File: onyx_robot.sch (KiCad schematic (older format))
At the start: 30 parts, among them P1 EXT1, P2 EXT2, P3 READER, P4 FTDI, Q1 Q_NMOS_GDS, Q2 Q_NMOS_GDS, SW2 RESET, U1 ADP2301, U2 RELAY_SPDT, U3 ESP-12E

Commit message: Swap 12V in/out connector pins
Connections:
- wire segments 106 -> 107
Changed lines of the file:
@@
 L +12V #PWR013
 U 1 1 55857384
-P 2275 3650
-F 0 "#PWR013" H 2275 3500 50  0001 C CNN
-F 1 "+12V" H 2275 3790 50  0000 C CNN
-F 2 "" H 2275 3650 60  0000 C CNN
-F 3 "" H 2275 3650 60  0000 C CNN
-	1    2275 3650
-	1    0    0    -1
-$EndComp
-Text GLabel 1650 3450 2    60   Input ~ 0
+P 1550 3350
+F 0 "#PWR013" H 1550 3200 50  0001 C CNN
+F 1 "+12V" H 1550 3490 50  0000 C CNN
+F 2 "" H 1550 3350 60  0000 C CNN
+F 3 "" H 1550 3350 60  0000 C CNN
+	1    1550 3350
+	1    0    0    -1
+$EndComp
+Text GLabel 1650 3650 2    60   Input ~ 0
 12V_OUT
 Text GLabel 1650 5100 2    60   Input ~ 0
@@
 Connection ~ 1550 5000
 Wire Wire Line
-	1450 3450 1650 3450
-Wire Wire Line
-	1450 3650 2275 3650
+	1450 3650 1650 3650
 Wire Wire Line
 	1450 3550 1550 3550
@@
 	4025 1800 4025 1525
 Connection ~ 4025 1525
+Wire Wire Line
+	1450 3450 1550 3450
+Wire Wire Line
+	1550 3450 1550 3350
 $EndSCHEMATC

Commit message: Switch to standard (not hand-soldering) footprints to save space
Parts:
- C1, C2: footprint Capacitors_SMD:C_1206_HandSoldering -> Capacitors_SMD:C_1206
- C3, C4: footprint Capacitors_SMD:C_0603_HandSoldering -> Capacitors_SMD:C_0603
- D1, D2: footprint Diodes_SMD:Diode-SMA_Handsoldering -> Diodes_SMD:Diode-SMA_Standard
- Q1, Q2: footprint Housings_SOT-23_SOT-143_TSOT-6:SOT-23_Handsoldering -> Housings_SOT-23_SOT-143_TSOT-6:SOT-23
- R1, R10, R11, R2, R3, R4, R5, R6, R7, R8, R9: footprint Resistors_SMD:R_0603_HandSoldering -> Resistors_SMD:R_0603
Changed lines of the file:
@@
 F 0 "R6" V 6905 4425 50  0000 C CNN
 F 1 "10K" V 6825 4425 50  0000 C CNN
-F 2 "Resistors_SMD:R_0603_HandSoldering" V 6755 4425 30  0001 C CNN
+F 2 "Resistors_SMD:R_0603" V 6755 4425 30  0001 C CNN
 F 3 "" H 6825 4425 30  0000 C CNN
 	1    6825 4425
@@
 F 0 "R10" V 9905 4675 50  0000 C CNN
 F 1 "10K" V 9825 4675 50  0000 C CNN
-F 2 "Resistors_SMD:R_0603_HandSoldering" V 9755 4675 30  0001 C CNN
+F 2 "Resistors_SMD:R_0603" V 9755 4675 30  0001 C CNN
 F 3 "" H 9825 4675 30  0000 C CNN
 	1    9825 4675
@@
 F 0 "R7" V 7130 1700 50  0000 C CNN
 F 1 "10K 1%" V 6975 1700 50  0000 C CNN
-F 2 "Resistors_SMD:R_0603_HandSoldering" V 6980 1700 30  0001 C CNN
+F 2 "Resistors_SMD:R_0603" V 6980 1700 30  0001 C CNN
 F 3 "" H 7050 1700 30  0000 C CNN
 	1    7050 1700
@@
 F 0 "R8" V 7130 2125 50  0000 C CNN
 F 1 "2K2 1%" V 6975 2125 50  0000 C CNN
-F 2 "Resistors_SMD:R_0603_HandSoldering" V 6980 2125 30  0001 C CNN
+F 2 "Resistors_SMD:R_0603" V 6980 2125 30  0001 C CNN
 F 3 "" H 7050 2125 30  0000 C CNN
 	1    7050 2125
@@
 F 0 "R11" V 10180 1600 50  0000 C CNN
 F 1 "10K" V 10100 1600 50  0000 C CNN
-F 2 "Resistors_SMD:R_0603_HandSoldering" V 10030 1600 30  0001 C CNN
+F 2 "Resistors_SMD:R_0603" V 10030 1600 30  0001 C CNN
 F 3 "" H 10100 1600 30  0000 C CNN
 	1    10100 1600
@@
 F 0 "R9" V 8780 1550 50  0000 C CNN
 F 1 "10K" V 8700 1550 50  0000 C CNN
-F 2 "Resistors_SMD:R_0603_HandSoldering" V 8630 1550 30  0001 C CNN
+F 2 "Resistors_SMD:R_0603" V 8630 1550 30  0001 C CNN
 F 3 "" H 8700 1550 30  0000 C CNN
 	1    8700 1550
@@
 F 0 "Q1" H 4125 4650 50  0000 R CNN
 F 1 "Q_NMOS_GDS" H 4475 4550 50  0000 R CNN
-F 2 "Housings_SOT-23_SOT-143_TSOT-6:SOT-23_Handsoldering" H 4025 4700 29  0001 C CNN
+F 2 "Housings_SOT-23_SOT-143_TSOT-6:SOT-23" H 4025 4700 29  0001 C CNN
 F 3 "" H 3825 4600 60  0000 C CNN
 	1    3825 4600
@@
 F 0 "D2" H 3925 4100 50  0000 C CNN
 F 1 "D" H 3925 3900 50  0000 C CNN
-F 2 "Diodes_SMD:Diode-SMA_Handsoldering" H 3925 4000 60  0001 C CNN
+F 2 "Diodes_SMD:Diode-SMA_Standard" H 3925 4000 60  0001 C CNN
 F 3 "" H 3925 4000 60  0000 C CNN
 	1    3925 4000
@@
 F 0 "R5" V 3655 4800 50  0000 C CNN
 F 1 "10K" V 3575 4800 50  0000 C CNN
-F 2 "Resistors_SMD:R_0603_HandSoldering" V 3505 4800 30  0001 C CNN
+F 2 "Resistors_SMD:R_0603" V 3505 4800 30  0001 C CNN
 F 3 "" H 3575 4800 30  0000 C CNN
 	1    3575 4800
@@
 F 0 "C1" H 1300 1800 50  0000 L CNN
 F 1 "10uF 25V" H 1075 1600 50  0000 L CNN
-F 2 "Capacitors_SMD:C_1206_HandSoldering" H 1313 1550 30  0001 C CNN
+F 2 "Capacitors_SMD:C_1206" H 1313 1550 30  0001 C CNN
 F 3 "" H 1275 1700 60  0000 C CNN
 	1    1275 1700
@@
 F 0 "R3" V 1655 1500 50  0000 C CNN
 F 1 "56K 1%" V 1500 1500 50  0000 C CNN
-F 2 "Resistors_SMD:R_0603_HandSoldering" V 1505 1500 30  0001 C CNN
+F 2 "Resistors_SMD:R_0603" V 1505 1500 30  0001 C CNN
 F 3 "" H 1575 1500 30  0000 C CNN
 	1    1575 1500
@@
 F 0 "R4" V 1655 2075 50  0000 C CNN
 F 1 "10K2 1%" V 1500 2075 50  0000 C CNN
-F 2 "Resistors_SMD:R_0603_HandSoldering" V 1505 2075 30  0001 C CNN
+F 2 "Resistors_SMD:R_0603" V 1505 2075 30  0001 C CNN
 F 3 "" H 1575 2075 30  0000 C CNN
 	1    1575 2075
@@
 F 0 "C3" H 2900 1475 50  0000 L CNN
 F 1 "0.1uF 6.3V" H 3000 1375 50  0000 L CNN
-F 2 "Capacitors_SMD:C_0603_HandSoldering" H 2913 1225 30  0001 C CNN
+F 2 "Capacitors_SMD:C_0603" H 2913 1225 30  0001 C CNN
 F 3 "" H 2875 1375 60  0000 C CNN
 	1    2875 1375
@@
 F 0 "C2" H 4050 2050 50  0000 L CNN
 F 1 "22uF 6.3V" H 4050 1850 50  0000 L CNN
-F 2 "Capacitors_SMD:C_1206_HandSoldering" H 4063 1800 30  0001 C CNN
+F 2 "Capacitors_SMD:C_1206" H 4063 1800 30  0001 C CNN
 F 3 "" H 4025 1950 60  0000 C CNN
 	1    4025 1950
@@
 F 0 "R1" V 3805 1675 50  0000 C CNN
 F 1 "31K6 1%" H 3500 1600 50  0000 C CNN
-F 2 "Resistors_SMD:R_0603_HandSoldering" V 3655 1675 30  0001 C CNN
+F 2 "Resistors_SMD:R_0603" V 3655 1675 30  0001 C CNN
 F 3 "" H 3725 1675 30  0000 C CNN
 	1    3725 1675
@@
 F 0 "R2" V 3805 2075 50  0000 C CNN
 F 1 "20K2 1%" V 3650 2075 50  0000 C CNN
-F 2 "Resistors_SMD:R_0603_HandSoldering" V 3655 2075 30  0001 C CNN
+F 2 "Resistors_SMD:R_0603" V 3655 2075 30  0001 C CNN
 F 3 "" H 3725 2075 30  0000 C CNN
 	1    3725 2075
@@
 F 0 "D1" H 2875 2175 50  0000 C CNN
 F 1 "B230A" H 2875 1975 50  0000 C CNN
-F 2 "Diodes_SMD:Diode-SMA_Handsoldering" H 2875 2075 60  0001 C CNN
+F 2 "Diodes_SMD:Diode-SMA_Standard" H 2875 2075 60  0001 C CNN
 F 3 "" H 2875 2075 60  0000 C CNN
 	1    2875 2075
@@
 F 0 "C4" H 6850 5025 50  0000 L CNN
 F 1 "0.1uF" H 6850 4825 50  0000 L CNN
-F 2 "Capacitors_SMD:C_0603_HandSoldering" H 6863 4775 30  0001 C CNN
+F 2 "Capacitors_SMD:C_0603" H 6863 4775 30  0001 C CNN
 F 3 "" H 6825 4925 60  0000 C CNN
 	1    6825 4925
@@
 F 0 "Q2" H 9250 1900 50  0000 R CNN
 F 1 "Q_NMOS_GDS" H 9600 1800 50  0000 R CNN
-F 2 "Housings_SOT-23_SOT-143_TSOT-6:SOT-23_Handsoldering" H 9150 1950 29  0001 C CNN
+F 2 "Housings_SOT-23_SOT-143_TSOT-6:SOT-23" H 9150 1950 29  0001 C CNN
 F 3 "" H 8950 1850 60  0000 C CNN
 	1    8950 1850

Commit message: Use corrected ESP-12E footprint
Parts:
- U3: footprint jdunmire-kicad-ESP8266:ESP-12E -> timhawes:ESP-12E
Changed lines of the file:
@@
 F 0 "U3" H 8600 4175 50  0000 C CNN
 F 1 "ESP-12E" H 8600 4375 50  0000 C CNN
-F 2 "jdunmire-kicad-ESP8266:ESP-12E" H 8600 4275 50  0001 C CNN
+F 2 "timhawes:ESP-12E" H 8600 4275 50  0001 C CNN
 F 3 "" H 8600 4275 50  0001 C CNN
 	1    8600 4275

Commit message: Shuffle READER pins to put GND/3.3V together
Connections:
- wire segments 107 -> 129
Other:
- moved on the sheet: P3, P4
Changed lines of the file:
@@
 L CONN_01X06 P4
 U 1 1 55847D6C
-P 2950 6525
-F 0 "P4" H 2950 6875 50  0000 C CNN
-F 1 "FTDI" V 3050 6525 50  0000 C CNN
-F 2 "Pin_Headers:Pin_Header_Straight_1x06" H 2950 6525 60  0001 C CNN
-F 3 "" H 2950 6525 60  0000 C CNN
-	1    2950 6525
+P 3100 6525
+F 0 "P4" H 3100 6875 50  0000 C CNN
+F 1 "FTDI" V 3200 6525 50  0000 C CNN
+F 2 "Pin_Headers:Pin_Header_Straight_1x06" H 3100 6525 60  0001 C CNN
+F 3 "" H 3100 6525 60  0000 C CNN
+	1    3100 6525
 	-1   0    0    1
 $EndComp
@@
 L CONN_01X08 P3
 U 1 1 55847F14
-P 1250 6425
-F 0 "P3" H 1250 6875 50  0000 C CNN
-F 1 "READER" V 1350 6425 50  0000 C CNN
-F 2 "timhawes:Terminal_Block_5.08mm_x8" H 1250 6425 60  0001 C CNN
-F 3 "" H 1250 6425 60  0000 C CNN
-	1    1250 6425
+P 1250 6525
+F 0 "P3" H 1250 6975 50  0000 C CNN
+F 1 "READER" V 1350 6525 50  0000 C CNN
+F 2 "timhawes:Terminal_Block_5.08mm_x8" H 1250 6525 60  0001 C CNN
+F 3 "" H 1250 6525 60  0000 C CNN
+	1    1250 6525
 	-1   0    0    1
 $EndComp
@@
 Text GLabel 9600 4075 2    60   Input ~ 0
 RX
-Text GLabel 3200 6475 2    60   Input ~ 0
+Text GLabel 3350 6475 2    60   Input ~ 0
 TX
-Text GLabel 3375 6375 2    60   Input ~ 0
+Text GLabel 3525 6375 2    60   Input ~ 0
 RX
 $Comp
 L +3.3V #PWR09
 U 1 1 5584AC0A
-P 3725 6575
-F 0 "#PWR09" H 3725 6425 50  0001 C CNN
-F 1 "+3.3V" H 3725 6715 50  0000 C CNN
-F 2 "" H 3725 6575 60  0000 C CNN
-F 3 "" H 3725 6575 60  0000 C CNN
-	1    3725 6575
+P 3875 6575
+F 0 "#PWR09" H 3875 6425 50  0001 C CNN
+F 1 "+3.3V" H 3875 6715 50  0000 C CNN
+F 2 "" H 3875 6575 60  0000 C CNN
+F 3 "" H 3875 6575 60  0000 C CNN
+	1    3875 6575
 	-1   0    0    -1
 $EndComp
-NoConn ~ 3150 6675
-NoConn ~ 3150 6275
-Text GLabel 1550 6475 2    60   Input ~ 0
+NoConn ~ 3300 6675
+NoConn ~ 3300 6275
+Text GLabel 1500 6475 2    60   Input ~ 0
 MOSI
-Text GLabel 1875 6575 2    60   Input ~ 0
+Text GLabel 1825 6575 2    60   Input ~ 0
 MISO
-Text GLabel 1875 6375 2    60   Input ~ 0
+Text GLabel 1825 6375 2    60   Input ~ 0
 CS
-Text GLabel 1550 6675 2    60   Input ~ 0
+Text GLabel 1500 6675 2    60   Input ~ 0
 CLK
-Text GLabel 1875 6175 2    60   Input ~ 0
+Text GLabel 1825 6175 2    60   Input ~ 0
 PIEZO
 $Comp
 L +3.3V #PWR010
 U 1 1 5584BDD3
-P 1550 5975
-F 0 "#PWR010" H 1550 5825 50  0001 C CNN
-F 1 "+3.3V" H 1550 6115 50  0000 C CNN
-F 2 "" H 1550 5975 60  0000 C CNN
-F 3 "" H 1550 5975 60  0000 C CNN
-	1    1550 5975
-	1    0    0    -1
-$EndComp
-Text GLabel 1550 6275 2    60   Input ~ 0
+P 2325 6675
+F 0 "#PWR010" H 2325 6525 50  0001 C CNN
+F 1 "+3.3V" H 2325 6815 50  0000 C CNN
+F 2 "" H 2325 6675 60  0000 C CNN
+F 3 "" H 2325 6675 60  0000 C CNN
+	1    2325 6675
+	1    0    0    -1
+$EndComp
+Text GLabel 1500 6275 2    60   Input ~ 0
 LED
 $Comp
@@
 L GND #PWR029
 U 1 1 558E4075
-P 3250 6875
-F 0 "#PWR029" H 3250 6625 50  0001 C CNN
-F 1 "GND" H 3250 6725 50  0000 C CNN
-F 2 "" H 3250 6875 60  0000 C CNN
-F 3 "" H 3250 6875 60  0000 C CNN
-	1    3250 6875
+P 3400 6875
+F 0 "#PWR029" H 3400 6625 50  0001 C CNN
+F 1 "GND" H 3400 6725 50  0000 C CNN
+F 2 "" H 3400 6875 60  0000 C CNN
+F 3 "" H 3400 6875 60  0000 C CNN
+	1    3400 6875
 	1    0    0    -1
 $EndComp
@@
 	7050 1550 7050 1500
 Wire Wire Line
-	7050 1850 7050 1975
+	7050 1850 7050 1900
+Wire Wire Line
+	7050 1900 7050 1975
 Wire Wire Line
 	7050 2275 7050 2350
@@
 	10100 1350 10100 1450
 Wire Wire Line
-	10100 1750 10100 1850
+	10100 1750 10100 1800
+Wire Wire Line
+	10100 1800 10100 1850
 Wire Wire Line
 	10400 1800 10100 1800
@@
 	10100 2450 10100 2550
 Wire Wire Line
-	6750 4675 7700 4675
+	6750 4675 6825 4675
+Wire Wire Line
+	6825 4675 7700 4675
 Wire Wire Line
 	7350 3975 7700 3975
@@
 	6825 4175 6825 4275
 Wire Wire Line
-	6825 4575 6825 4775
+	6825 4575 6825 4675
+Wire Wire Line
+	6825 4675 6825 4775
 Connection ~ 6825 4675
 Wire Wire Line
-	9500 4675 9675 4675
+	9500 4675 9575 4675
+Wire Wire Line
+	9575 4675 9675 4675
 Wire Wire Line
 	9575 4675 9575 4750
@@
 	7700 4075 7625 4075
 Wire Wire Line
-	9500 4575 10300 4575
+	9500 4575 10125 4575
+Wire Wire Line
+	10125 4575 10300 4575
 Wire Wire Line
 	9825 3975 9500 3975
@@
 	9600 4475 9500 4475
 Wire Wire Line
-	3375 6375 3150 6375
-Wire Wire Line
-	3725 6575 3150 6575
-Wire Wire Line
-	3475 4600 3625 4600
+	3525 6375 3300 6375
+Wire Wire Line
+	3875 6575 3300 6575
+Wire Wire Line
+	3475 4600 3575 4600
+Wire Wire Line
+	3575 4600 3625 4600
 Wire Wire Line
 	3575 4600 3575 4650
 Connection ~ 3575 4600
 Wire Wire Line
-	3925 4800 3925 5050
+	3925 4800 3925 5000
+Wire Wire Line
+	3925 5000 3925 5050
 Wire Wire Line
 	3575 4950 3575 5000
@@
 	3925 4150 3925 4400
 Wire Wire Line
-	3925 3525 3925 3850
+	3925 3525 3925 3600
+Wire Wire Line
+	3925 3600 3925 3850
 Wire Wire Line
 	3925 3850 4100 3850
@@
 	5425 4150 5375 4150
 Wire Wire Line
-	1275 1100 1275 1550
+	1275 1100 1275 1225
+Wire Wire Line
+	1275 1225 1275 1550
 Connection ~ 1275 1225
 Wire Wire Line
@@
 Connection ~ 1575 1225
 Wire Wire Line
-	1575 1650 1575 1925
+	1575 1650 1575 1825
+Wire Wire Line
+	1575 1825 1575 1925
 Wire Wire Line
 	1575 1825 1725 1825
 Connection ~ 1575 1825
 Wire Wire Line
-	1575 2225 1575 2325
+	1575 2225 1575 2275
+Wire Wire Line
+	1575 2275 1575 2325
 Wire Wire Line
 	1275 1850 1275 2275
@@
 	2725 1225 2875 1225
 Wire Wire Line
-	2725 1525 3050 1525
+	2725 1525 2875 1525
+Wire Wire Line
+	2875 1525 3050 1525
 Wire Wire Line
 	2875 1525 2875 1925
@@
 Connection ~ 2875 1525
 Wire Wire Line
-	3650 1525 4300 1525
+	3650 1525 3725 1525
+Wire Wire Line
+	3725 1525 4025 1525
+Wire Wire Line
+	4025 1525 4300 1525
 Connection ~ 3725 1525
 Connection ~ 3725 1825
@@
 	4025 2100 4025 2325
 Wire Wire Line
-	1275 1225 1725 1225
+	1275 1225 1575 1225
+Wire Wire Line
+	1575 1225 1725 1225
 Wire Wire Line
 	1275 2275 1575 2275
@@
 	9050 2050 9050 2150
 Wire Wire Line
-	8550 1850 8750 1850
-Wire Wire Line
-	8700 1700 8700 2000
+	8550 1850 8700 1850
+Wire Wire Line
+	8700 1850 8750 1850
+Wire Wire Line
+	8700 1700 8700 1850
+Wire Wire Line
+	8700 1850 8700 2000
 Connection ~ 8700 1850
 Wire Wire Line
@@
 	8700 2600 8700 2700
 Wire Wire Line
-	3150 6775 3250 6775
-Wire Wire Line
-	3250 6775 3250 6875
-Wire Wire Line
-	3200 6475 3150 6475
+	3300 6775 3400 6775
+Wire Wire Line
+	3400 6775 3400 6875
+Wire Wire Line
+	3350 6475 3300 6475
 Wire Wire Line
 	1450 3850 1650 3850
@@
 Connection ~ 1550 3750
 Wire Wire Line
-	1550 3550 1550 4050
+	1550 3550 1550 3750
+Wire Wire Line
+	1550 3750 1550 3950
+Wire Wire Line
+	1550 3950 1550 4050
 Wire Wire Line
 	1450 3950 1550 3950
 Connection ~ 1550 3950
 Wire Wire Line
-	1550 4800 1550 5325
+	1550 4800 1550 5000
+Wire Wire Line
+	1550 5000 1550 5200
+Wire Wire Line
+	1550 5200 1550 5325
 Wire Wire Line
 	1450 5200 1550 5200
@@
 L GND #PWR032
 U 1 1 558E6A71
-P 1550 6875
-F 0 "#PWR032" H 1550 6625 50  0001 C CNN
-F 1 "GND" H 1550 6725 50  0000 C CNN
-F 2 "" H 1550 6875 60  0000 C CNN
-F 3 "" H 1550 6875 60  0000 C CNN
-	1    1550 6875
-	1    0    0    -1
-$EndComp
-Wire Wire Line
-	1450 6775 1550 6775
-Wire Wire Line
-	1550 6775 1550 6875
-Wire Wire Line
-	1450 6075 1550 6075
-Wire Wire Line
-	1550 6075 1550 5975
-Wire Wire Line
-	1875 6175 1450 6175
-Wire Wire Line
-	1450 6275 1550 6275
-Wire Wire Line
-	1450 6375 1875 6375
-Wire Wire Line
-	1450 6475 1550 6475
-Wire Wire Line
-	1450 6575 1875 6575
-Wire Wire Line
-	1450 6675 1550 6675
+P 1550 6975
+F 0 "#PWR032" H 1550 6725 50  0001 C CNN
+F 1 "GND" H 1550 6825 50  0000 C CNN
+F 2 "" H 1550 6975 60  0000 C CNN
+F 3 "" H 1550 6975 60  0000 C CNN
+	1    1550 6975
+	1    0    0    -1
+$EndComp
+Wire Wire Line
+	1450 6875 1550 6875
+Wire Wire Line
+	1550 6875 1550 6975
+Wire Wire Line
+	1450 6775 2325 6775
+Wire Wire Line
+	2325 6775 2325 6675
+Wire Wire Line
+	1825 6175 1450 6175
+Wire Wire Line
+	1450 6275 1500 6275
+Wire Wire Line
+	1450 6375 1825 6375
+Wire Wire Line
+	1450 6475 1500 6475
+Wire Wire Line
+	1450 6575 1825 6575
+Wire Wire Line
+	1450 6675 1500 6675
 Wire Wire Line
 	3725 1825 2725 1825

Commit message: Swap power in/out pins
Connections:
- wire segments 129 -> 107
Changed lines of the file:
@@
 L +12V #PWR013
 U 1 1 55857384
-P 1550 3350
-F 0 "#PWR013" H 1550 3200 50  0001 C CNN
-F 1 "+12V" H 1550 3490 50  0000 C CNN
-F 2 "" H 1550 3350 60  0000 C CNN
-F 3 "" H 1550 3350 60  0000 C CNN
-	1    1550 3350
-	1    0    0    -1
-$EndComp
-Text GLabel 1650 3650 2    60   Input ~ 0
+P 2100 3600
+F 0 "#PWR013" H 2100 3450 50  0001 C CNN
+F 1 "+12V" H 2100 3740 50  0000 C CNN
+F 2 "" H 2100 3600 60  0000 C CNN
+F 3 "" H 2100 3600 60  0000 C CNN
+	1    2100 3600
+	1    0    0    -1
+$EndComp
+Text GLabel 1650 3850 2    60   Input ~ 0
 12V_OUT
 Text GLabel 1650 5100 2    60   Input ~ 0
@@
 Text GLabel 1650 4700 2    60   Input ~ 0
 TAMPER
-Text GLabel 1650 3850 2    60   Input ~ 0
+Text GLabel 1650 3450 2    60   Input ~ 0
 SNIB
 $Comp
@@
 	7050 1550 7050 1500
 Wire Wire Line
-	7050 1850 7050 1900
-Wire Wire Line
-	7050 1900 7050 1975
+	7050 1850 7050 1975
 Wire Wire Line
 	7050 2275 7050 2350
@@
 	10100 1350 10100 1450
 Wire Wire Line
-	10100 1750 10100 1800
-Wire Wire Line
-	10100 1800 10100 1850
+	10100 1750 10100 1850
 Wire Wire Line
 	10400 1800 10100 1800
@@
 	10100 2450 10100 2550
 Wire Wire Line
-	6750 4675 6825 4675
-Wire Wire Line
-	6825 4675 7700 4675
+	6750 4675 7700 4675
 Wire Wire Line
 	7350 3975 7700 3975
@@
 	6825 4175 6825 4275
 Wire Wire Line
-	6825 4575 6825 4675
-Wire Wire Line
-	6825 4675 6825 4775
+	6825 4575 6825 4775
 Connection ~ 6825 4675
 Wire Wire Line
-	9500 4675 9575 4675
-Wire Wire Line
-	9575 4675 9675 4675
+	9500 4675 9675 4675
 Wire Wire Line
 	9575 4675 9575 4750
@@
 	7700 4075 7625 4075
 Wire Wire Line
-	9500 4575 10125 4575
-Wire Wire Line
-	10125 4575 10300 4575
+	9500 4575 10300 4575
 Wire Wire Line
 	9825 3975 9500 3975
@@
 	3875 6575 3300 6575
 Wire Wire Line
-	3475 4600 3575 4600
-Wire Wire Line
-	3575 4600 3625 4600
+	3475 4600 3625 4600
 Wire Wire Line
 	3575 4600 3575 4650
 Connection ~ 3575 4600
 Wire Wire Line
-	3925 4800 3925 5000
-Wire Wire Line
-	3925 5000 3925 5050
+	3925 4800 3925 5050
 Wire Wire Line
 	3575 4950 3575 5000
@@
 	3925 4150 3925 4400
 Wire Wire Line
-	3925 3525 3925 3600
-Wire Wire Line
-	3925 3600 3925 3850
+	3925 3525 3925 3850
 Wire Wire Line
 	3925 3850 4100 3850
@@
 	5425 4150 5375 4150
 Wire Wire Line
-	1275 1100 1275 1225
-Wire Wire Line
-	1275 1225 1275 1550
+	1275 1100 1275 1550
 Connection ~ 1275 1225
 Wire Wire Line
@@
 Connection ~ 1575 1225
 Wire Wire Line
-	1575 1650 1575 1825
-Wire Wire Line
-	1575 1825 1575 1925
+	1575 1650 1575 1925
 Wire Wire Line
 	1575 1825 1725 1825
 Connection ~ 1575 1825
 Wire Wire Line
-	1575 2225 1575 2275
-Wire Wire Line
-	1575 2275 1575 2325
+	1575 2225 1575 2325
 Wire Wire Line
 	1275 1850 1275 2275
@@
 	2725 1225 2875 1225
 Wire Wire Line
-	2725 1525 2875 1525
-Wire Wire Line
-	2875 1525 3050 1525
+	2725 1525 3050 1525
 Wire Wire Line
 	2875 1525 2875 1925
@@
 Connection ~ 2875 1525
 Wire Wire Line
-	3650 1525 3725 1525
-Wire Wire Line
-	3725 1525 4025 1525
-Wire Wire Line
-	4025 1525 4300 1525
+	3650 1525 4300 1525
 Connection ~ 3725 1525
 Connection ~ 3725 1825
@@
 	4025 2100 4025 2325
 Wire Wire Line
-	1275 1225 1575 1225
-Wire Wire Line
-	1575 1225 1725 1225
+	1275 1225 1725 1225
 Wire Wire Line
 	1275 2275 1575 2275
@@
 	9050 2050 9050 2150
 Wire Wire Line
-	8550 1850 8700 1850
-Wire Wire Line
-	8700 1850 8750 1850
-Wire Wire Line
-	8700 1700 8700 1850
-Wire Wire Line
-	8700 1850 8700 2000
+	8550 1850 8750 1850
+Wire Wire Line
+	8700 1700 8700 2000
 Connection ~ 8700 1850
 Wire Wire Line
@@
 Connection ~ 1550 5000
 Wire Wire Line
-	1450 3650 1650 3650
+	1450 3650 2100 3650
 Wire Wire Line
 	1450 3550 1550 3550
@@
 Connection ~ 1550 3750
 Wire Wire Line
-	1550 3550 1550 3750
-Wire Wire Line
-	1550 3750 1550 3950
-Wire Wire Line
-	1550 3950 1550 4050
+	1550 3550 1550 4050
 Wire Wire Line
 	1450 3950 1550 3950
 Connection ~ 1550 3950
 Wire Wire Line
-	1550 4800 1550 5000
-Wire Wire Line
-	1550 5000 1550 5200
-Wire Wire Line
-	1550 5200 1550 5325
+	1550 4800 1550 5325
 Wire Wire Line
 	1450 5200 1550 5200
@@
 Connection ~ 4025 1525
 Wire Wire Line
-	1450 3450 1550 3450
-Wire Wire Line
-	1550 3450 1550 3350
+	1450 3450 1650 3450
+Wire Wire Line
+	2100 3650 2100 3600
 $EndSCHEMATC

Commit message: Clean-up silkscreen labels
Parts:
- JP2: value PROG -> BOOT
- renumbered SW2 to SW1
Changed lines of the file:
@@
 ADC
 $Comp
-L SW_PUSH SW2
+L SW_PUSH SW1
 U 1 1 55848A10
 P 10100 2150
-F 0 "SW2" H 10250 2260 50  0000 C CNN
+F 0 "SW1" H 10250 2260 50  0000 C CNN
 F 1 "RESET" H 10100 2070 50  0000 C CNN
 F 2 "timhawes:EVQPT5" H 10100 2150 60  0001 C CNN
@@
 P 8700 2300
 F 0 "JP2" H 8700 2450 50  0000 C CNN
-F 1 "PROG" H 8700 2220 50  0000 C CNN
+F 1 "BOOT" H 8700 2220 50  0000 C CNN
 F 2 "Pin_Headers:Pin_Header_Straight_1x02" H 8700 2300 60  0001 C CNN
 F 3 "" H 8700 2300 60  0000 C CNN

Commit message: Change MOSFET SOT-23 pin ordering and adjust layout to match
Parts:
- Q1, Q2: value Q_NMOS_GDS -> Q_NMOS_GSD; symbol Q_NMOS_GDS -> Q_NMOS_GSD
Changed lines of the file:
@@
 $EndComp
 $Comp
-L Q_NMOS_GDS Q1
+L Q_NMOS_GSD Q1
 U 1 1 55855319
 P 3825 4600
 F 0 "Q1" H 4125 4650 50  0000 R CNN
-F 1 "Q_NMOS_GDS" H 4475 4550 50  0000 R CNN
+F 1 "Q_NMOS_GSD" H 4475 4550 50  0000 R CNN
 F 2 "Housings_SOT-23_SOT-143_TSOT-6:SOT-23" H 4025 4700 29  0001 C CNN
 F 3 "" H 3825 4600 60  0000 C CNN
@@
 SNIB
 $Comp
-L Q_NMOS_GDS Q2
+L Q_NMOS_GSD Q2
 U 1 1 558DCA88
 P 8950 1850
 F 0 "Q2" H 9250 1900 50  0000 R CNN
-F 1 "Q_NMOS_GDS" H 9600 1800 50  0000 R CNN
+F 1 "Q_NMOS_GSD" H 9600 1800 50  0000 R CNN
 F 2 "Housings_SOT-23_SOT-143_TSOT-6:SOT-23" H 9150 1950 29  0001 C CNN
 F 3 "" H 8950 1850 60  0000 C CNN

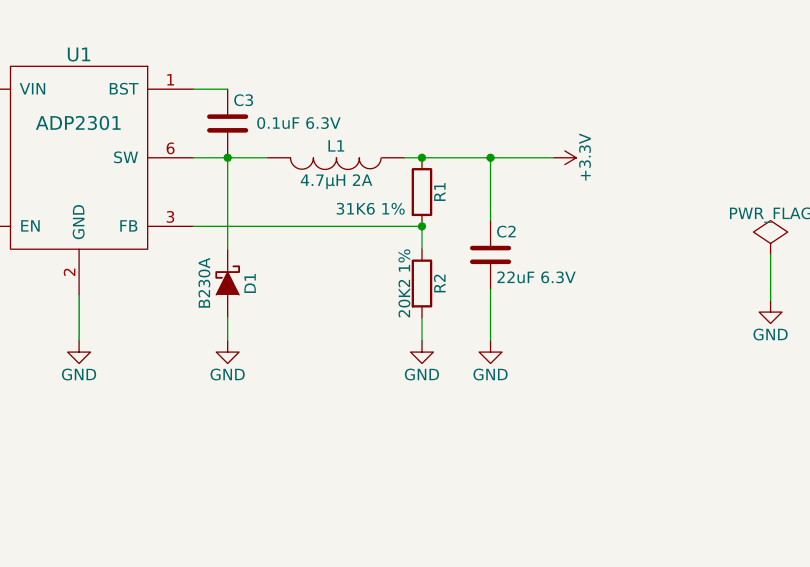
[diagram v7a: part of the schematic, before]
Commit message: Correction to value of R2
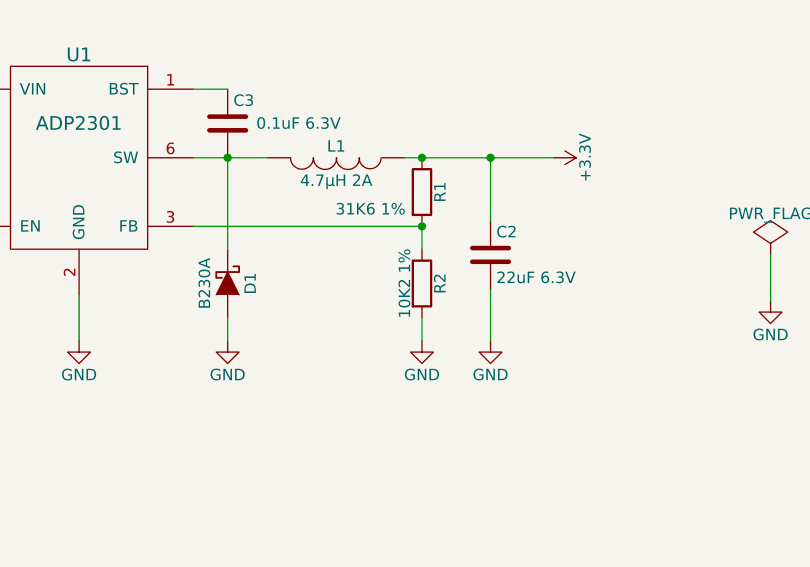
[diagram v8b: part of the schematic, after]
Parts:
- R2: value 20K2 1% -> 10K2 1%
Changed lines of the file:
@@
 P 3725 2075
 F 0 "R2" V 3805 2075 50  0000 C CNN
-F 1 "20K2 1%" V 3650 2075 50  0000 C CNN
+F 1 "10K2 1%" V 3650 2075 50  0000 C CNN
 F 2 "Resistors_SMD:R_0603" V 3655 2075 30  0001 C CNN
 F 3 "" H 3725 2075 30  0000 C CNN
